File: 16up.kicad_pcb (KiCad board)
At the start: 2 copper layers, 60.8 x 99.9 mm, 37 parts, among them CN1 EXPANSION_PORT, CN2 ALMOST_USERPORT, CN3 DB9_MALE, CN4 TAPE_IN, J1 ATTENTION_IN, U1 GAL20V8, U102 74LS652, U2 MOS_6529, U3 MOS_6551_ACIA, U4 MAX238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

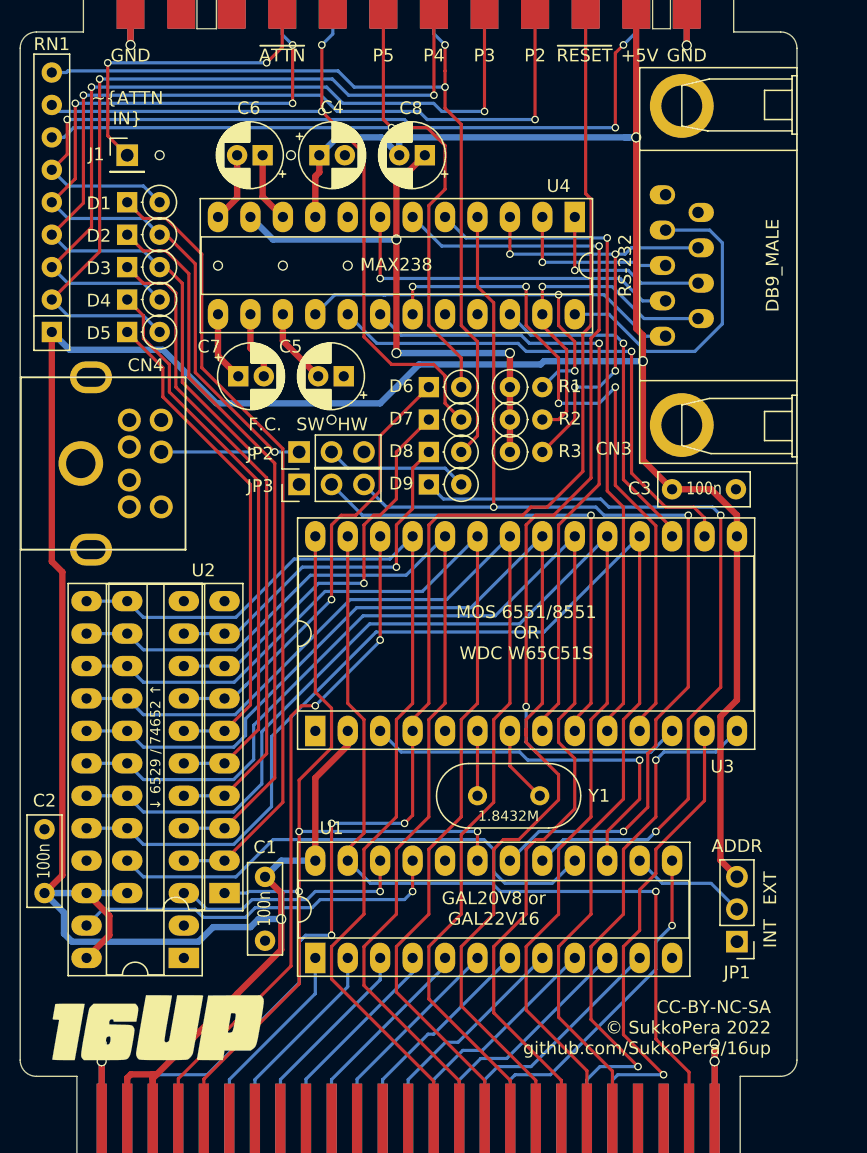
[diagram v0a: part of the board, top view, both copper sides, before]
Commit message: Move crystal above U3 for easier insertion These crystals are always too tall...
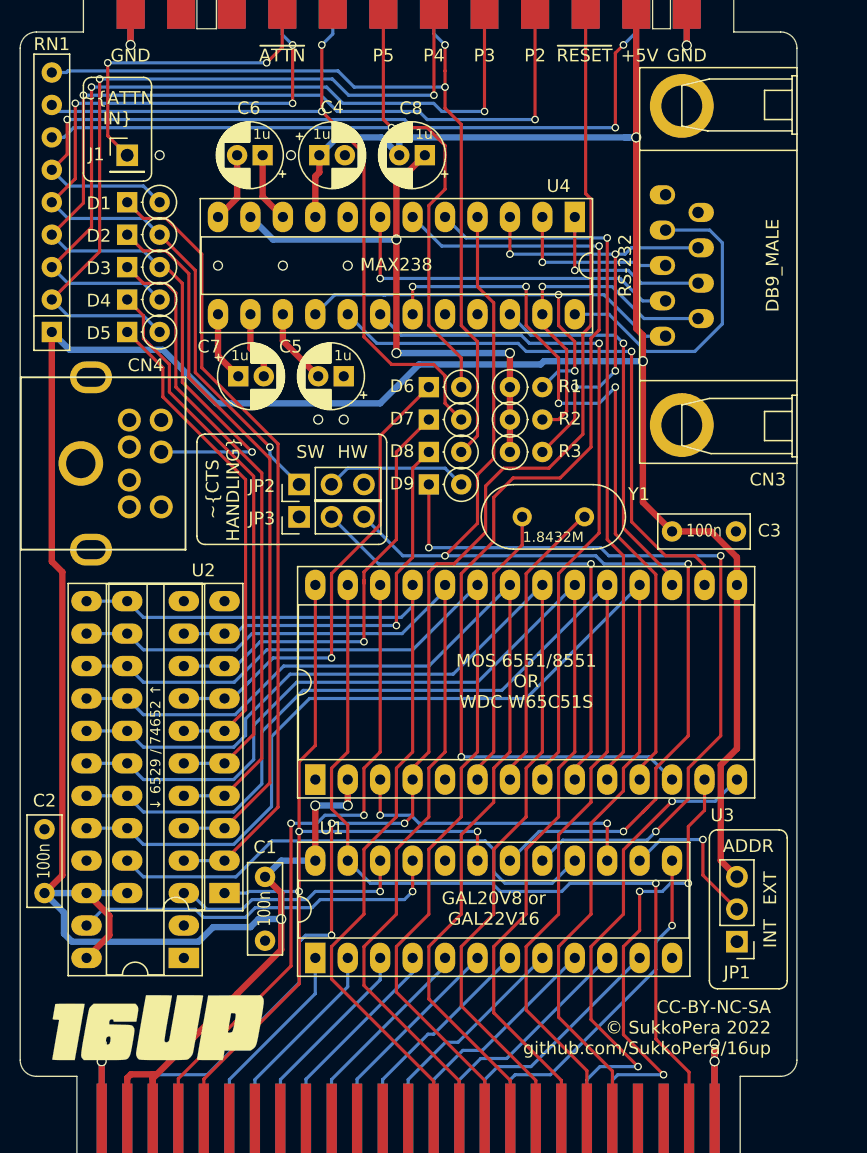
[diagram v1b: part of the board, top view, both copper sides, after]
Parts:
- moved Y1 22.1 mm to (166.0, 95.6)
- moved U3 3.81 mm to (144.9, 116.2)
- moved C3 3.30 mm to (172.8, 96.8)
- moved JP3 2.54 mm to (143.6, 95.6)
- moved JP2 2.54 mm to (143.6, 93.1)
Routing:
- net Net-(U3-Pad6): track 5.08 -> 22.0 mm
- net Net-(U3-Pad7): track 6.94 -> 23.1 mm
- net /rxd_ttl: track 70.0 -> 79.4 mm
- net /d3: track 99.0 -> 90.3 mm
- net /~cs_ser: track 31.1 -> 23.8 mm, vias 1 -> 2
- net /d2: track 101.3 -> 94.5 mm
- net /d0: track 109.2 -> 102.9 mm
- net /d4: track 91.6 -> 86.2 mm
- net /d5: track 88.2 -> 82.8 mm
- net /d1: track 104.1 -> 98.7 mm
- net /d6: track 84.9 -> 79.7 mm
- net /r_~w: track 75.1 -> 70.2 mm
- net /d7: track 81.5 -> 77.1 mm
- net /a1: track 43.7 -> 39.5 mm
- net /~rts_ttl: track 50.3 -> 54.1 mm
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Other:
- board text added: "1u"
- board text added: "NOTES: - ON PLUS/4 USE EXTERNAL ADDRESS ONLY (ACIA = $FD6x, 6529 = $FD7x) - ON C16 INTERNAL ADDRESS REQUIRES MODIFICATION (ACIA = $FD0x, 6529 = $FD1x) - HW ~CTS~ HANDLING REQUIRES W65C51S ACIA - DO NOT MOUNT RN1 IF USING ORIGINAL MOS 6529 - REPLACE D1-8 WITH 0-OHM RESISTORS IF USING ORIGINAL MOS 6529 OR 74x654 REPLACEMENT"
- board text added: "~CTS HANDLING"
- board text removed: "F.C."
- board text removed: "NOTES: - ON PLUS/4 USE EXTERNAL ADDRESS ONLY (ACIA = $FD6x, 6529 = $FD7x) - ON C16 INTERNAL ADDRESS REQUIRES MODIFICATION (ACIA = $FD0x, 6529 = $FD1x) - HW FLOW CONTROL REQUIRES W65C51S ACIA - DO NOT MOUNT RN1 IF USING ORIGINAL MOS 6529 - REPLACE D1-8 WITH 0-OHM RESISTORS IF USING ORIGINAL MOS 6529 OR 74x654 REPLACEMENT"

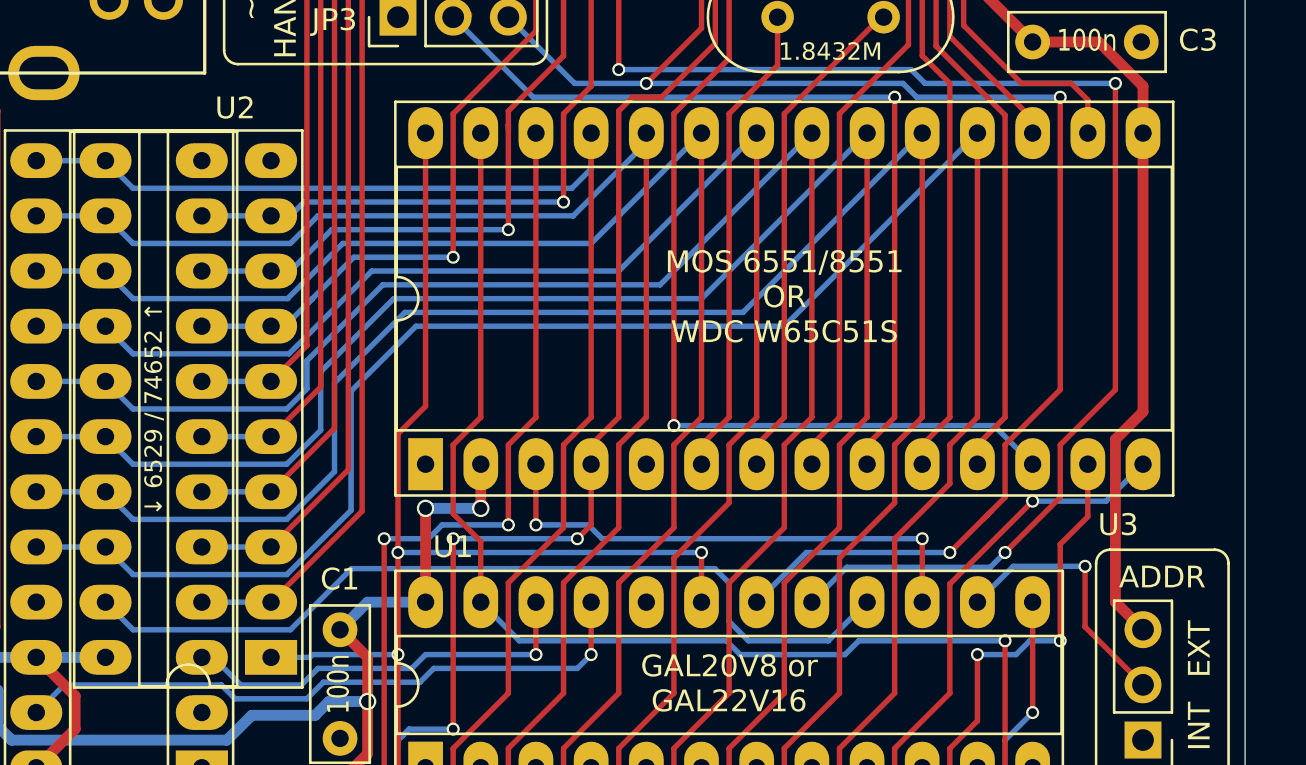
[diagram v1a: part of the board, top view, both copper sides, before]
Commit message: Improve ground plane
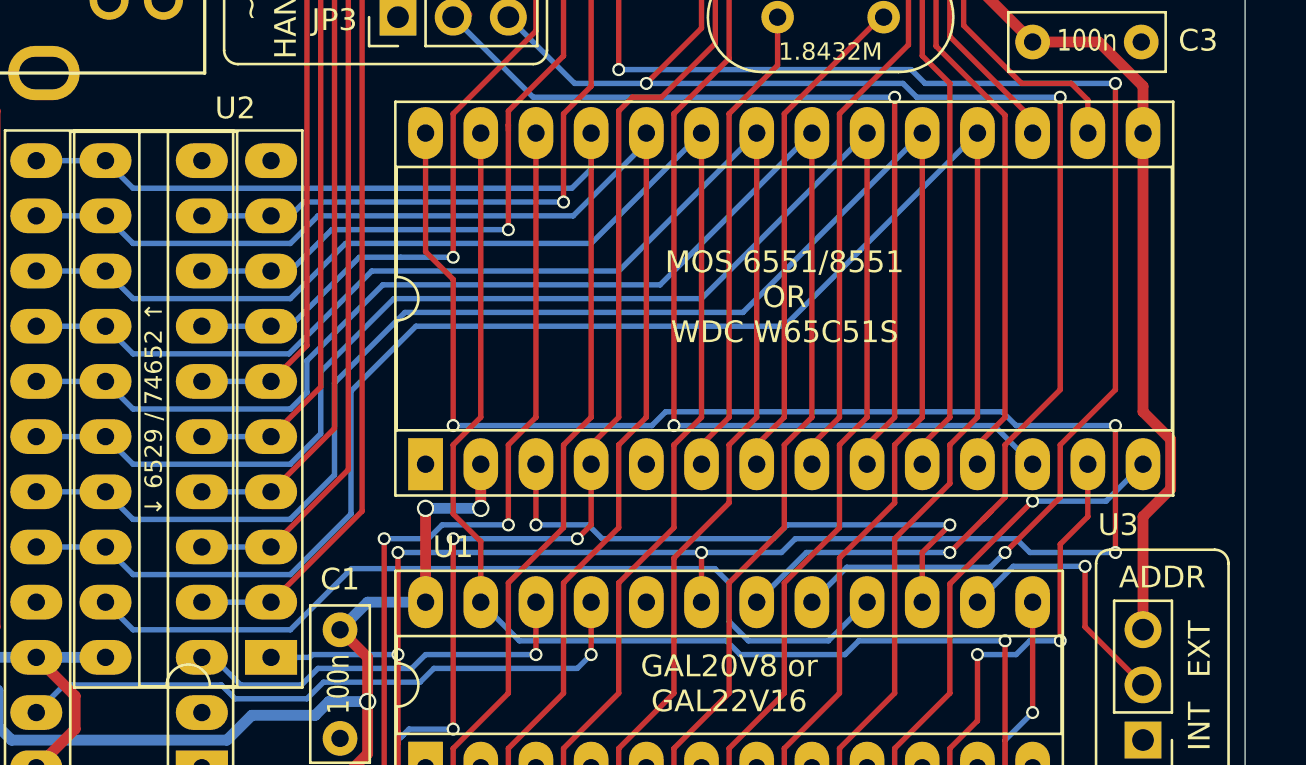
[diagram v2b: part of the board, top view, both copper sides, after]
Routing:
- net /r_~w: track 70.2 -> 120.8 mm, vias 3 -> 6
- net /~cs_ser: track 23.8 -> 26.5 mm

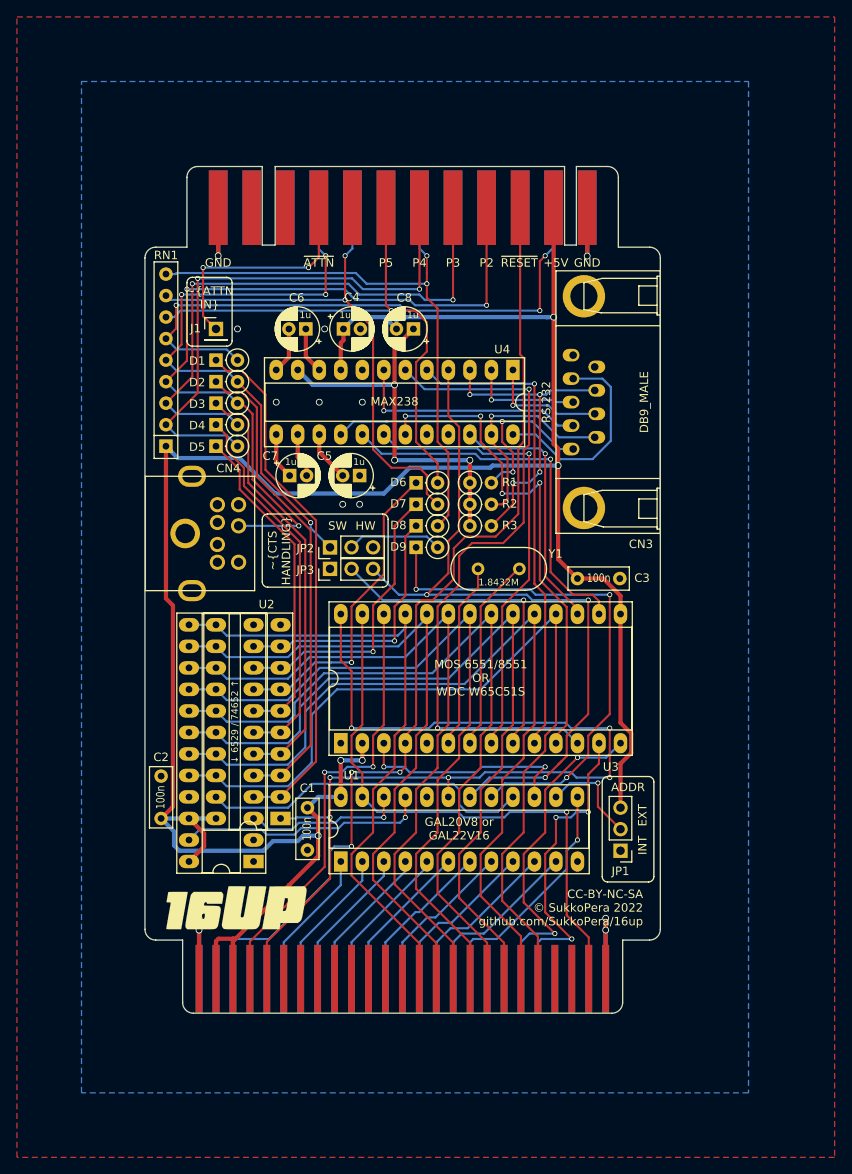
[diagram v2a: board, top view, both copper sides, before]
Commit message: Only support 74x654 as 6529 replacement
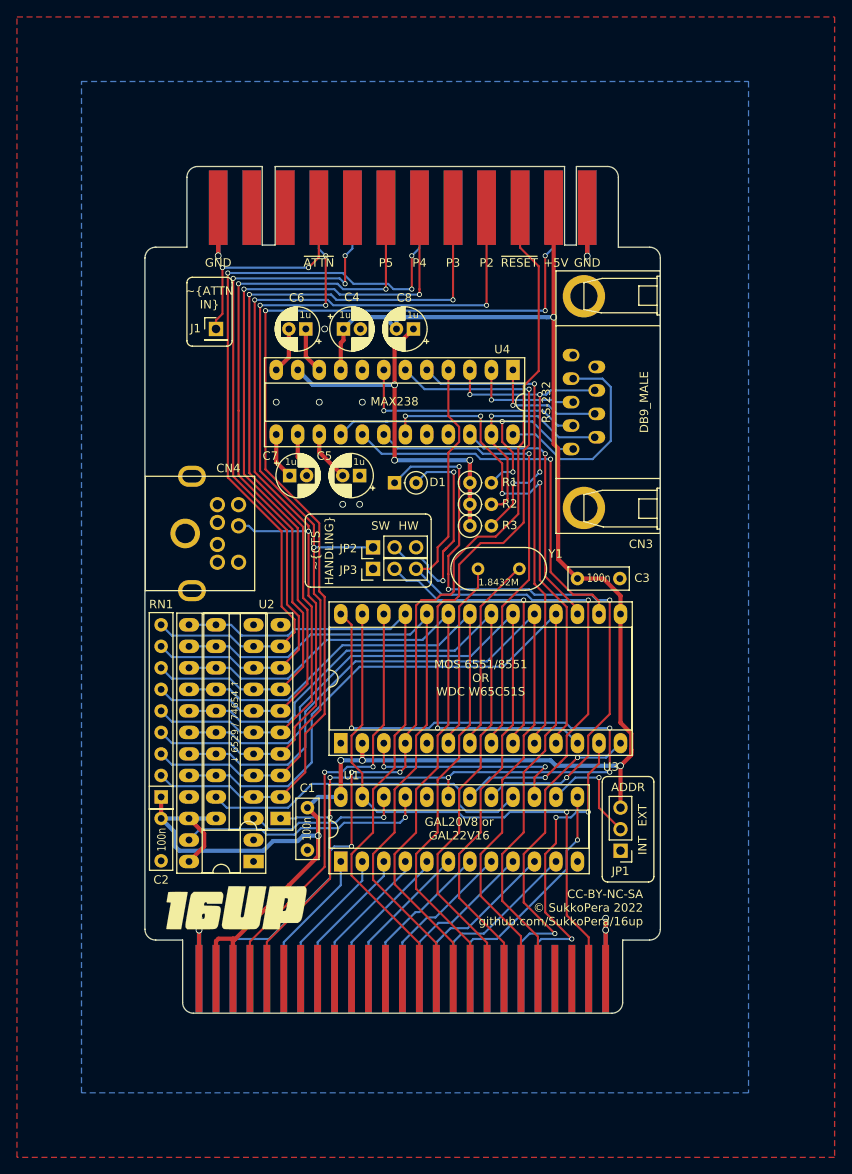
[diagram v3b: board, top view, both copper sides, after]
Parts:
- removed the D1 at (130.2, 71.0)
- removed D2, D3, D4, D5, D6, D7, D8: BAT43, Diode_THT:D_DO-35_SOD27_P2.54mm_Vertical_KathodeUp
- moved RN1 41.4 mm to (123.7, 122.6)
- moved D1 8.03 mm to (151.3, 85.5)
- moved JP2 5.08 mm to (148.7, 93.1)
- moved JP3 5.08 mm to (148.7, 95.6)
- turned C2 to 270 degrees
- renumbered D9 to D1
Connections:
- CN2 pad 4: /pc2 -> /p2
- CN2 pad 5: /pc3 -> /p3
- CN2 pad 6: /pc4 -> /p4
- CN2 pad 7: /pc5 -> /p5
- CN2 pad B: /pc0 -> /p0
- CN2 pad F: /pc7 -> /p7
- CN2 pad J: /pc6 -> /p6
- CN2 pad K: /pc1 -> /p1
- CN4 pad 7: /pc2 -> /p2
- JP2 pad 1: /pc1 -> /p1
- RN1 pad 2: /pc4 -> /p0
- RN1 pad 3: /pc3 -> /p1
- RN1 pad 4: /pc2 -> /p2
- RN1 pad 5: /pc1 -> /p3
- RN1 pad 6: /pc0 -> /p4
- RN1 pad 7: /pc5 -> /p5
- RN1 pad 8: /pc6 -> /p6
- RN1 pad 9: /pc7 -> /p7
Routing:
- net /pc2: track 93.9 -> 0.00 mm, vias 3 -> 0
- net /pc7: track 70.9 -> 0.00 mm, vias 2 -> 0
- net /pc0: track 70.0 -> 0.00 mm, vias 3 -> 0
- net /p2: track 51.2 -> 121.1 mm, vias 0 -> 3
- net /pc1: track 69.6 -> 0.00 mm, vias 4 -> 0
- net /pc3: track 67.3 -> 0.00 mm, vias 2 -> 0
- net /pc4: track 64.6 -> 0.00 mm, vias 2 -> 0
- net /pc5: track 64.6 -> 0.00 mm, vias 1 -> 0
- net /p7: track 31.5 -> 95.6 mm, vias 1 -> 3
- net /pc6: track 63.2 -> 0.00 mm, vias 2 -> 0
- net /p3: track 44.5 -> 106.6 mm, vias 0 -> 2
- net /p4: track 38.9 -> 100.6 mm, vias 0 -> 2
- net +5V: track 289.0 -> 227.8 mm
- net /p0: track 62.4 -> 123.2 mm, vias 0 -> 3
- net /p5: track 38.1 -> 95.4 mm, vias 1 -> 2
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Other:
- board text added: "NOTES: - ON PLUS/4 USE EXTERNAL ADDRESS ONLY (ACIA = $FD6x, 6529 = $FD7x) - ON C16 INTERNAL ADDRESS REQUIRES MODIFICATION (ACIA = $FD0x, 6529 = $FD1x) - HW ~CTS~ HANDLING REQUIRES W65C51S ACIA - DO NOT MOUNT RN1 IF USING ORIGINAL MOS 6529"
- board text added: "↓ 6529 / 74654 ↑"
- board text removed: "NOTES: - ON PLUS/4 USE EXTERNAL ADDRESS ONLY (ACIA = $FD6x, 6529 = $FD7x) - ON C16 INTERNAL ADDRESS REQUIRES MODIFICATION (ACIA = $FD0x, 6529 = $FD1x) - HW ~CTS~ HANDLING REQUIRES W65C51S ACIA - DO NOT MOUNT RN1 IF USING ORIGINAL MOS 6529 - REPLACE D1-8 WITH 0-OHM RESISTORS IF USING ORIGINAL MOS 6529 OR 74x654 REPLACEMENT"
- board text removed: "↓ 6529 / 74652 ↑"

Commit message: Start 232-less version
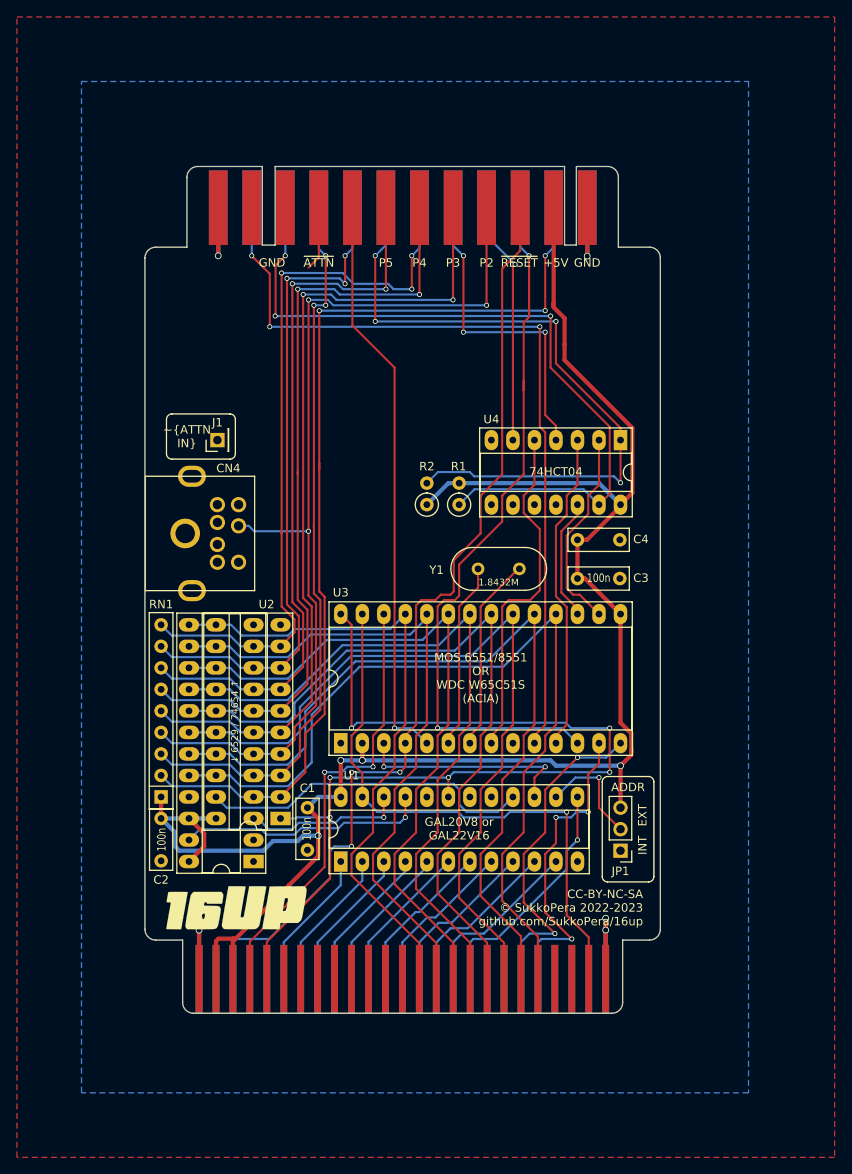
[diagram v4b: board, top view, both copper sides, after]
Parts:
- removed C5, C6, C7, C8: 1u, Capacitor_THT:CP_Radial_D5.0mm_P2.00mm
- removed CN3: DB9_MALE, 16up:DB_9M
- removed D1: BAT43, Diode_THT:D_DO-35_SOD27_P2.54mm_Vertical_KathodeUp
- removed JP2: JMP_CTS_IN, Connector_PinHeader_2.54mm:PinHeader_1x03_P2.54mm_Vertical
- removed JP3: JMP_CTS_ACIA, Connector_PinHeader_2.54mm:PinHeader_1x03_P2.54mm_Vertical
- removed R3: 10k, Resistor_THT:R_Axial_DIN0207_L6.3mm_D2.5mm_P2.54mm_Vertical
- C4: value 1u -> 100n; footprint Capacitor_THT:CP_Radial_D5.0mm_P2.00mm -> Capacitor_THT:C_Disc_D7.0mm_W2.5mm_P5.00mm
- U4: value MAX238 -> 74HCT04; footprint Package_DIP:DIP-24_W7.62mm_Socket_LongPads -> Package_DIP:DIP-14_W7.62mm_Socket_LongPads
- moved C4 37.2 mm to (172.8, 92.2)
- moved U4 15.2 mm to (177.9, 80.4)
- moved J1 13.1 mm to (130.3, 80.4), turned to 90 degrees
- moved R2 5.08 mm to (155.1, 88.1), turned to 90 degrees
- moved R1 2.88 mm to (158.9, 88.1), turned to 90 degrees
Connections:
- CN2 pad 8: Net-(CN2-Pad8) -> /rxc
- CN2 pad C: Net-(CN2-PadC) -> /rxd_ttl
- CN2 pad D: Net-(CN2-PadD) -> /rts_ttl
- CN2 pad E: Net-(CN2-PadE) -> /dtr_ttl
- CN2 pad H: Net-(CN2-PadH) -> /dcd_ttl
- CN2 pad L: Net-(CN2-PadL) -> /dsr_ttl
- CN2 pad M: Net-(CN2-PadM) -> /txd_ttl
- R1 pad 1: +12V -> /dsr_ttl
- R1 pad 2: /~dcd -> +5V
- R2 pad 1: +12V -> +5V
- R2 pad 2: /~dsr -> /dcd_ttl
- U1 pad 17: /cts_ttl -> Net-(U1-Pad17)
- U1 pad 18: /~cts_ttl -> Net-(U1-Pad18)
- U3 pad 5: Net-(U3-Pad5) -> /rxc
- U3 pad 9: Net-(JP3-Pad2) -> GND
- U4 pad 1: /~rts -> /dcd_ttl
- U4 pad 11: +12V -> Net-(U4-Pad11)
- U4 pad 12: Net-(C6-Pad2) -> /~dsr_ttl
- U4 pad 13: Net-(C7-Pad1) -> /dsr_ttl
- U4 pad 14: Net-(C7-Pad2) -> +5V
- U4 pad 2: /txd -> /~dcd_ttl
- U4 pad 3: /~cts -> /~dtr_ttl
- U4 pad 4: /~cts_ttl -> /dtr_ttl
- U4 pad 5: /txd_ttl -> /~rts_ttl
- U4 pad 6: /rxd_ttl -> /rts_ttl
- U4 pad 7: /rxd -> GND
- U4 pad 8: GND -> Net-(U4-Pad8)
- U4 pad 9: +5V -> Net-(U4-Pad9)
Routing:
- net /dsr_ttl: track 0.00 -> 89.5 mm, vias 0 -> 3
- net /~cts_ttl: track 82.4 -> 0.00 mm, vias 2 -> 0
- net /dcd_ttl: track 0.00 -> 81.4 mm, vias 0 -> 4
- net /cts_ttl: track 75.9 -> 0.00 mm, vias 4 -> 0
- net /rxc: track 0.00 -> 68.0 mm, vias 0 -> 1
- net +12V: track 45.2 -> 0.00 mm, vias 3 -> 0
- net /txd_ttl: track 56.8 -> 96.8 mm, vias 1 -> 3
- net /~dcd: track 39.2 -> 0.00 mm, vias 2 -> 0
- net /dtr_ttl: track 0.00 -> 38.9 mm, vias 0 -> 3
- net /~cts: track 36.7 -> 0.00 mm, vias 4 -> 0
- net Net-(JP3-Pad2): track 34.2 -> 0.00 mm, vias 1 -> 0
- net /rts_ttl: track 0.00 -> 28.9 mm, vias 0 -> 1
- net /rxd: track 27.9 -> 0.00 mm, vias 1 -> 0
- net Net-(D1-Pad2): track 26.6 -> 0.00 mm, vias 2 -> 0
- net /~dsr: track 26.0 -> 0.00 mm, vias 1 -> 0
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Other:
- board text added: "CC-BY-NC-SA © SukkoPera 2022-2023 github.com/SukkoPera/16up"
- board text added: "MOS 6551/8551 OR WDC W65C51S (ACIA)"
- board text added: "NOTES: - ON PLUS/4 USE EXTERNAL ADDRESS ONLY (ACIA = $FD6x, 6529 = $FD7x) - ON C16 INTERNAL ADDRESS REQUIRES MODIFICATION (ACIA = $FD0x, 6529 = $FD1x) - DO NOT MOUNT RN1 IF USING ORIGINAL MOS 6529"
- board text added: "V3"
- board text removed: "1u"
- board text removed: "CC-BY-NC-SA © SukkoPera 2022 github.com/SukkoPera/16up"
- board text removed: "HW"
- board text removed: "MOS 6551/8551 OR WDC W65C51S"
- board text removed: "NOTES: - ON PLUS/4 USE EXTERNAL ADDRESS ONLY (ACIA = $FD6x, 6529 = $FD7x) - ON C16 INTERNAL ADDRESS REQUIRES MODIFICATION (ACIA = $FD0x, 6529 = $FD1x) - HW ~CTS~ HANDLING REQUIRES W65C51S ACIA - DO NOT MOUNT RN1 IF USING ORIGINAL MOS 6529"
- board text removed: "RS-232"
- board text removed: "SW"
- board text removed: "V2"
- board text removed: "~CTS HANDLING"
